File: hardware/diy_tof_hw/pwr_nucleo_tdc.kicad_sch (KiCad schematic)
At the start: 35 parts, among them IC1 TDC7200PWR, IC2 TDC7200PWR, J1 Conn_01x02_Pin, J2 Conn_01x03_Pin, J3 Conn_01x02_Pin, SW1 SW_Nidec_CAS-120A1, U1 NUCLEO-F042K6, X1 SG-5032CAN

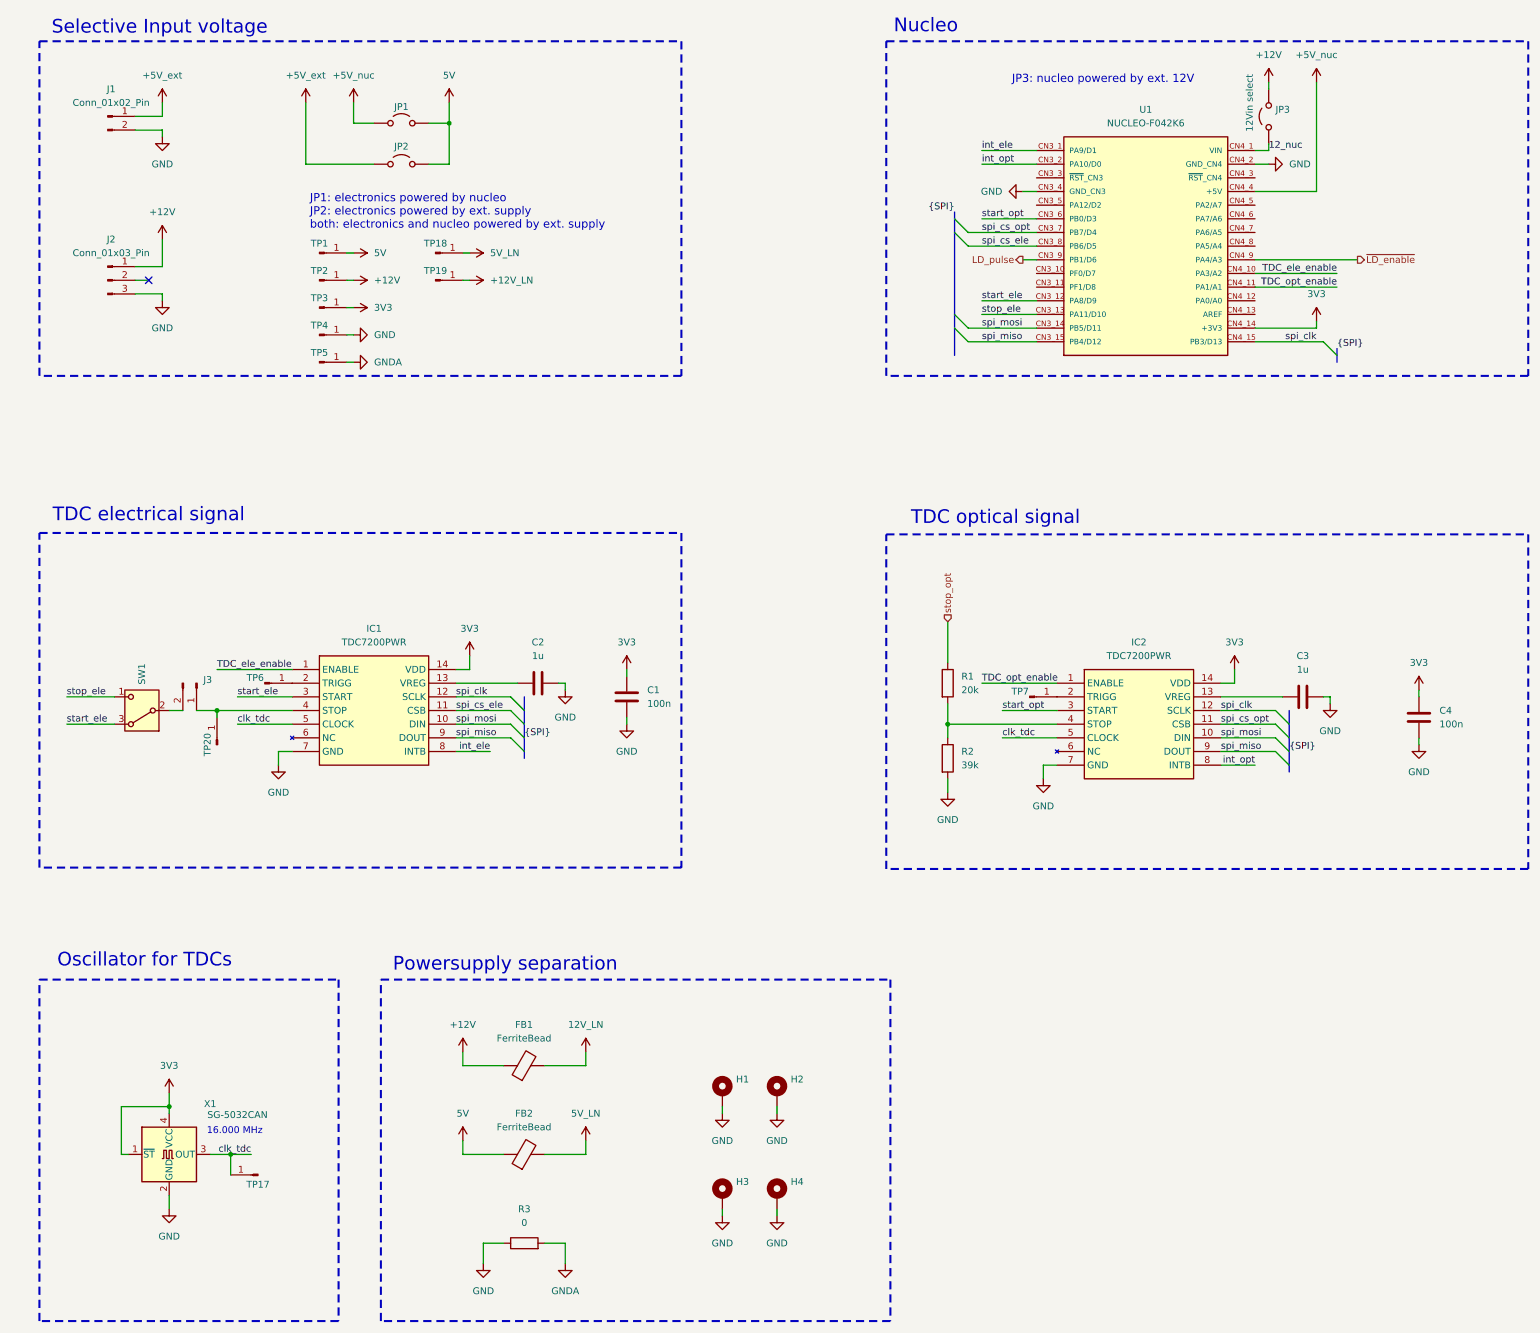
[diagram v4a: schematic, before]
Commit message: [hardware] placed all components, some minor renaming (got rid of the "+" in front of all source-labels)
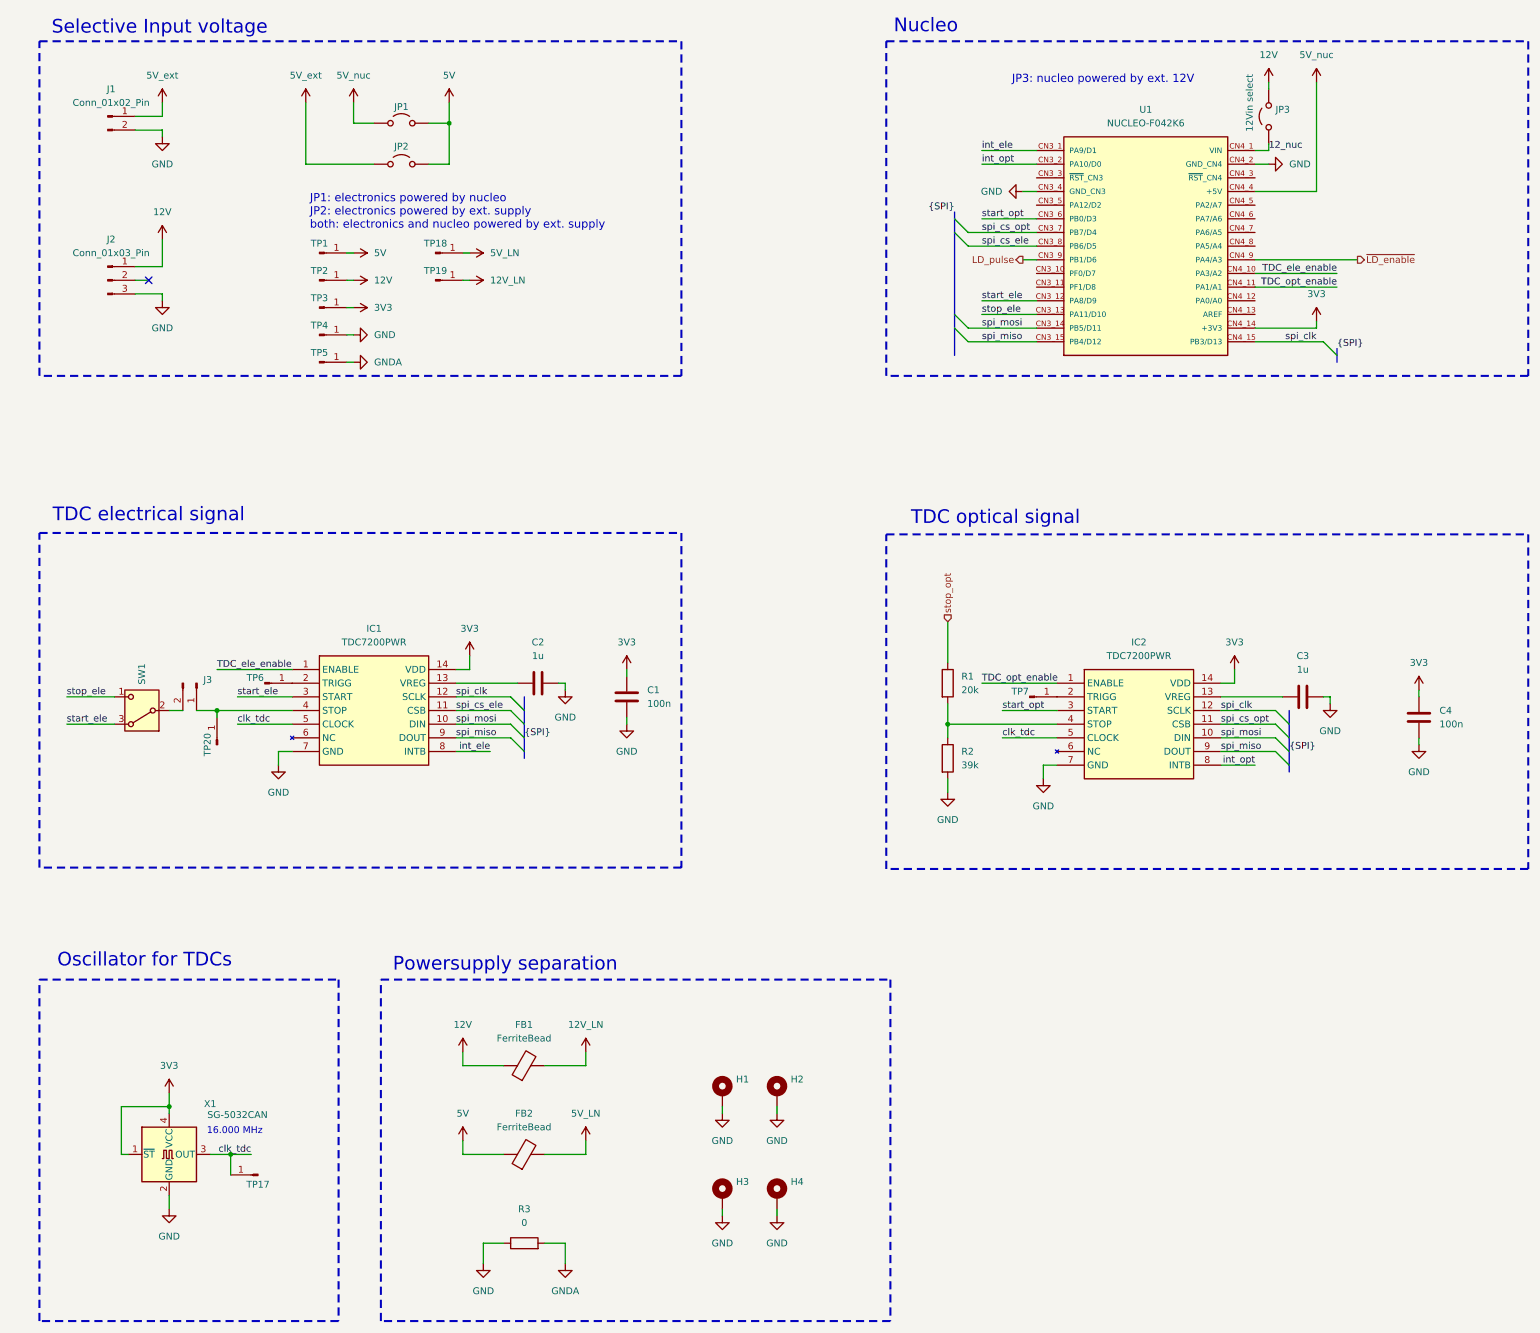
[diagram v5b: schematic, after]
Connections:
- net +12V_LN is gone; now on net 12V_LN: TP19.1 (Pin_1)
- net +12V renamed 12V
- net +5V_ext renamed 5V_ext
- net +5V_nuc renamed 5V_nuc
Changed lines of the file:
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@@
 			)
 		)
-		(property "Value" "+12V_LN"
+		(property "Value" "12V_LN"
 			(at 116.84 69.8499 90)
 			(effects
@@
 			)
 		)
-		(property "Value" "+12V"
+		(property "Value" "12V"
 			(at 95.25 69.8499 90)
 			(effects
@@
 			)
 		)
-		(property "Value" "+12V"
+		(property "Value" "12V"
 			(at 111.76 208.28 0)
 			(effects
@@
 			)
 		)
-		(property "Value" "+5V_ext"
+		(property "Value" "5V_ext"
 			(at 55.88 31.75 0)
 			(effects
@@
 			)
 		)
-		(property "Value" "+12V"
+		(property "Value" "12V"
 			(at 55.88 57.15 0)
 			(effects
@@
 			)
 		)
-		(property "Value" "+5V_nuc"
+		(property "Value" "5V_nuc"
 			(at 91.44 31.75 0)
 			(effects
@@
 			)
 		)
-		(property "Value" "+5V_nuc"
+		(property "Value" "5V_nuc"
 			(at 270.51 27.94 0)
 			(effects
@@
 			)
 		)
-		(property "Value" "+5V_ext"
+		(property "Value" "5V_ext"
 			(at 82.55 31.75 0)
 			(effects
@@
 			)
 		)
-		(property "Value" "+12V"
+		(property "Value" "12V"
 			(at 261.62 27.94 0)
 			(effects

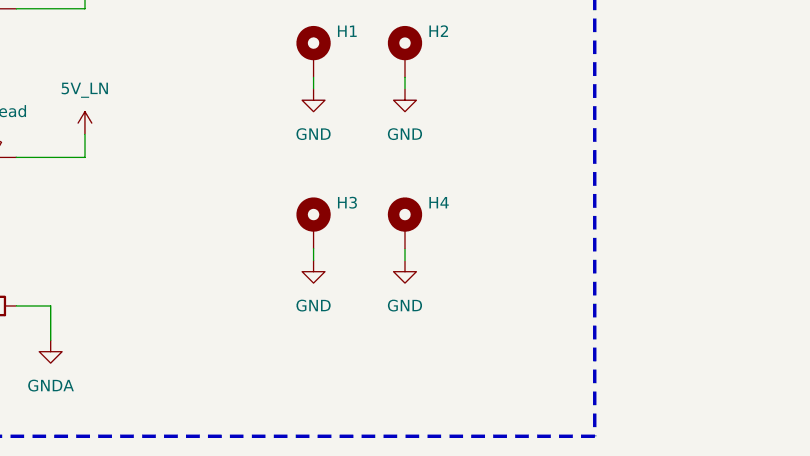
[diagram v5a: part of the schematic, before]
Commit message: [hardware] review findings  - moved powerplanes to layer In1  - added ground planes on all other layers  - rerouting of signals around the nucleo board, leaving enough space for ground fills
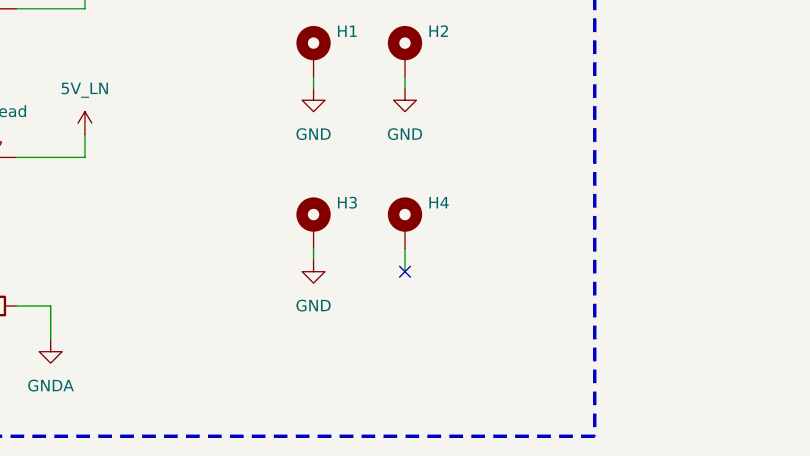
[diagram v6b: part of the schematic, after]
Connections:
- net GND: no longer H4.1
- no-connect marks 1 -> 2
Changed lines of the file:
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@@
 		(at 53.34 69.85)
+	)
+	(no_connect
+		(at 170.18 245.11)
 	)
 	(bus_entry
@@
 	(wire
 		(pts
+			(xy 170.18 245.11) (xy 170.18 242.57)
+		)
+		(stroke
+			(width 0)
+			(type default)
+		)
+	)
+	(wire
+		(pts
 			(xy 55.88 67.31) (xy 55.88 62.23)
 		)
@@
 		(pts
 			(xy 259.08 81.28) (xy 271.78 81.28)
-		)
-		(stroke
-			(width 0)
-			(type default)
-		)
-	)
-	(wire
-		(pts
-			(xy 170.18 243.84) (xy 170.18 242.57)
 		)
 		(stroke
@@
 					(unit 1)
 				)
-			)
-		)
-	)
-	(symbol
-		(lib_id "power:GND")
-		(at 170.18 243.84 0)
-		(unit 1)
-		(exclude_from_sim no)
-		(in_bom yes)
-		(on_board yes)
-		(dnp no)
-		(fields_autoplaced yes)
-		(property "Reference" "#PWR074"
-			(at 170.18 250.19 0)
-			(effects
-				(font
-					(size 1.27 1.27)
-				)
-				(hide yes)
-			)
-		)
-		(property "Value" "GND"
-			(at 170.18 248.92 0)
-			(effects
-				(font
-					(size 1.27 1.27)
-				)
-			)
-		)
-		(property "Footprint" ""
-			(at 170.18 243.84 0)
-			(effects
-				(font
-					(size 1.27 1.27)
-				)
-				(hide yes)
-			)
-		)
-		(property "Datasheet" ""
-			(at 170.18 243.84 0)
-			(effects
-				(font
-					(size 1.27 1.27)
-				)
-				(hide yes)
-			)
-		)
-		(property "Description" "Power symbol creates a global label with name \"GND\" , ground"
-			(at 170.18 243.84 0)
-			(effects
-				(font
-					(size 1.27 1.27)
-				)
-				(hide yes)
-			)
-		)
-		(pin "1"
-		)
-		(instances
-			(project "diy_tof_hw"
-				(path "/0f7bf370-0a80-4101-a61d-d850fd66ab1d/e3345fca-f581-4274-8897-90c8927ce695"
-					(reference "#PWR074")
-					(unit 1)
-				)

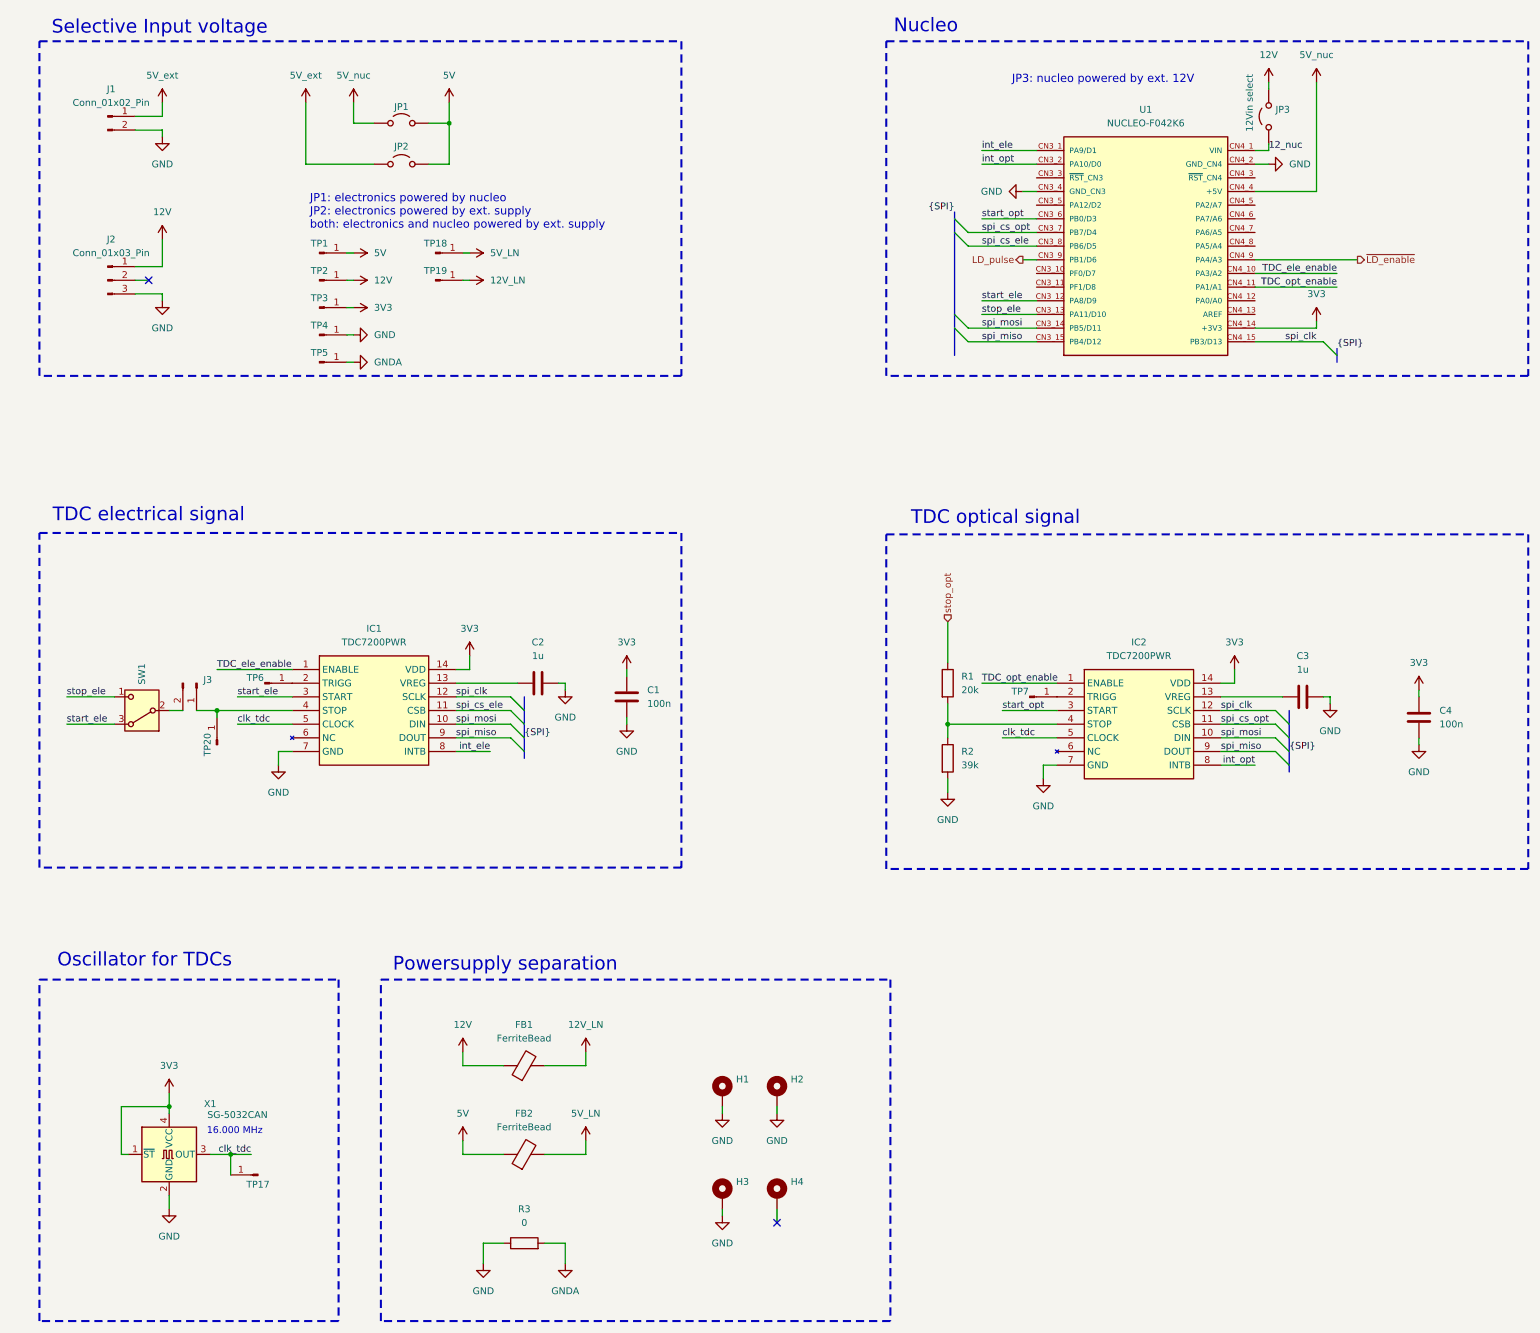
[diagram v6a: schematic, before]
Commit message: [hardware] further review findings  - adjusted some more traces  - one via per power pad  - added caps for a pi filter (dnp)  - added pullups for the CS signals of both TDCs
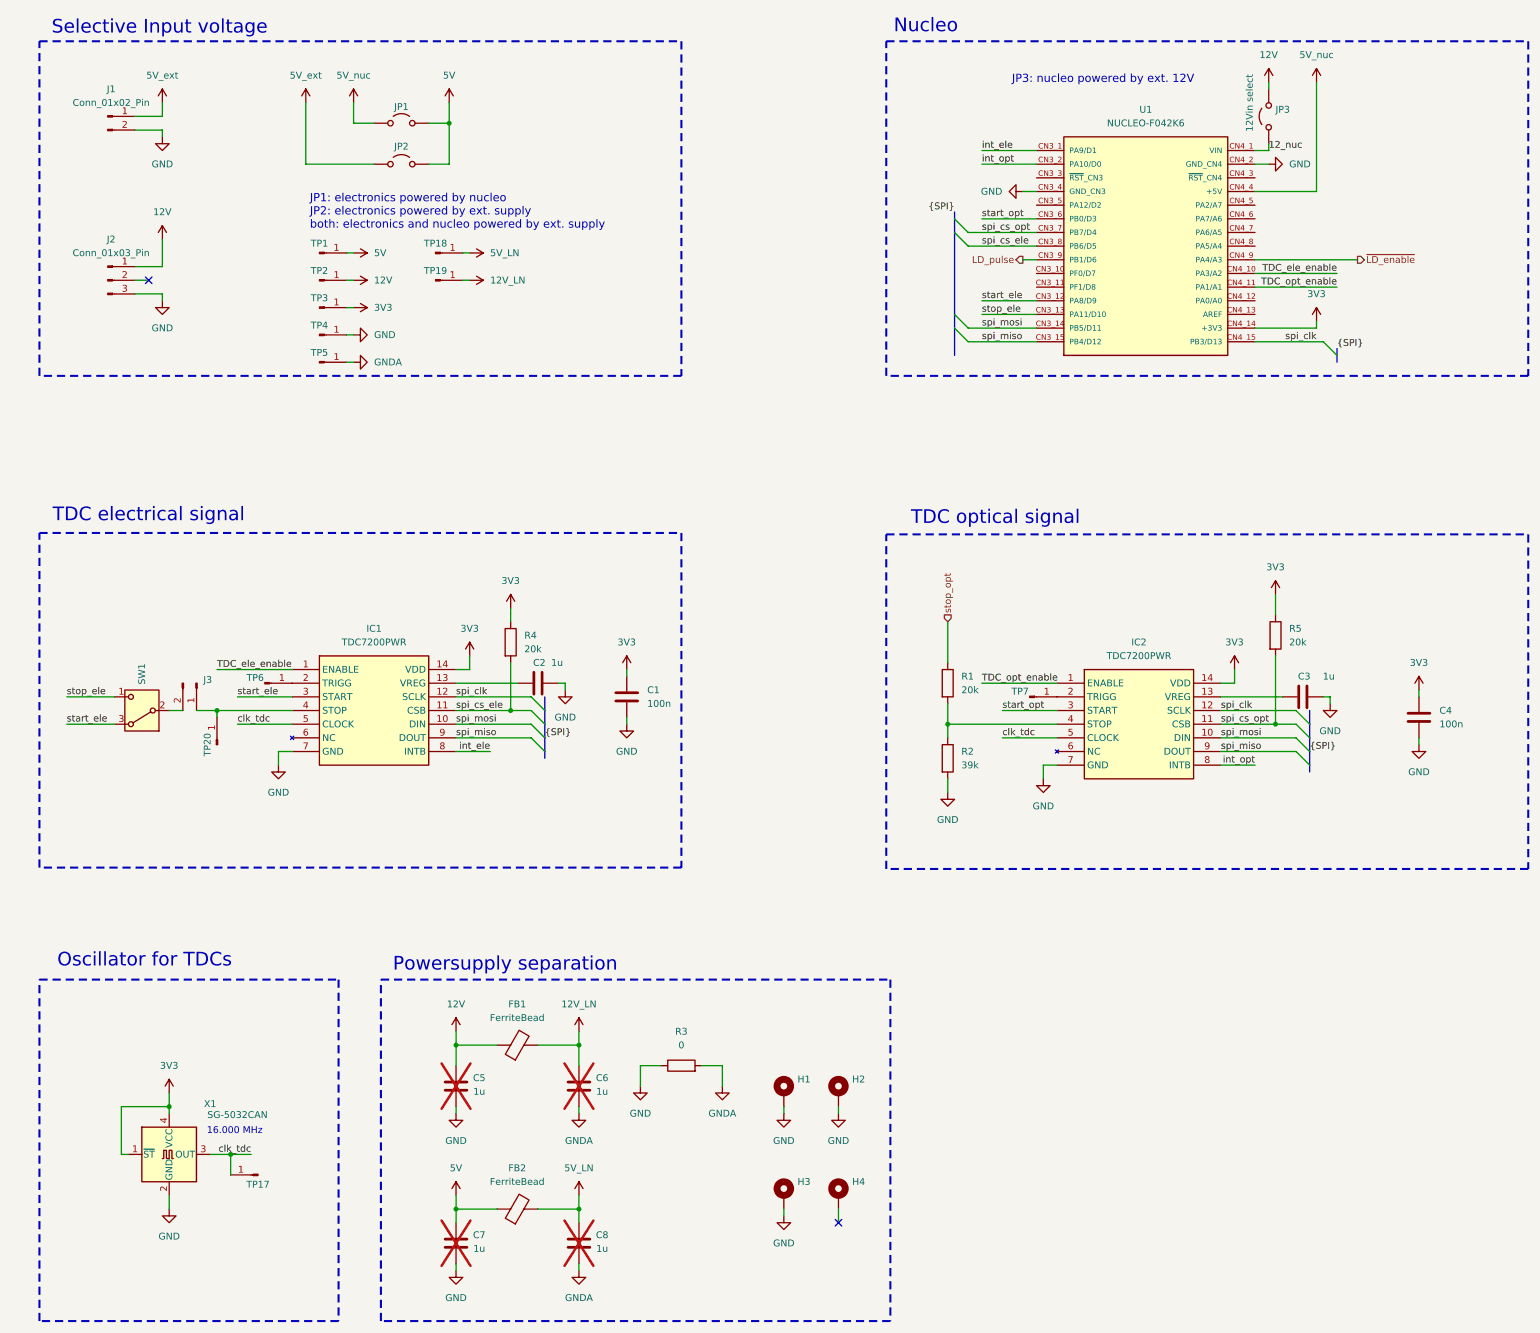
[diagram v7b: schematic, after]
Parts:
- added C5, C6, C7, C8: 1u, Capacitor_SMD:C_0402_1005Metric_Pad0.74x0.62mm_HandSolder, symbol Device:C
- added R4, R5: 20k, Resistor_SMD:R_0402_1005Metric_Pad0.72x0.64mm_HandSolder, symbol Device:R
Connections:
- net 12V: now also C5.2
- net 12V_LN: now also C6.2
- net 3V3: now also R4.1, R5.1
- net 5V: now also C7.2
- net 5V_LN: now also C8.2
- net GND: now also C5.1, C7.1
- net GNDA: now also C6.1, C8.1
- net spi_cs_ele: now also R4.2
- net spi_cs_opt: now also R5.2
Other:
- moved on the sheet: FB1, FB2, H1, H2, H3, H4, R3

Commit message: [hardware] release v1.0
Signed-off-by: Timon Burkard <burkard.timon@gmail.com>
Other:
- company: (none) -> OST
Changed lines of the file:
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@@
 	(title_block
 		(title "Power, Nucleo, TDC")
-		(rev "0.1")
+		(date "2024-12-27")
+		(rev "1.0")
+		(company "OST")
 		(comment 2 "schematics")
-		(comment 3 "w.i.p.")
+		(comment 3 "released")
 		(comment 8 "M. Schär")
+		(comment 9 "T. Burkard")
 	)
 	(bus_alias "SPI"
